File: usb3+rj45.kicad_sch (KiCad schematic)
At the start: 67 parts, among them J8 RJE361882415, T1 Trans_SM453229-381N7Y, T2 Trans_SM453229-381N7Y, T3 Trans_SM453229-381N7Y, T4 Trans_SM453229-381N7Y, T5 Choke_SRF2012A-801Y, T6 Choke_SRF2012A-801Y, T7 Choke_SRF2012A-801Y, T8 Choke_SRF2012A-801Y, U14 AP22615A_TSOT26, U15 ESD204DQAR, U16 ESD204DQAR, U17 AP22615A_TSOT26

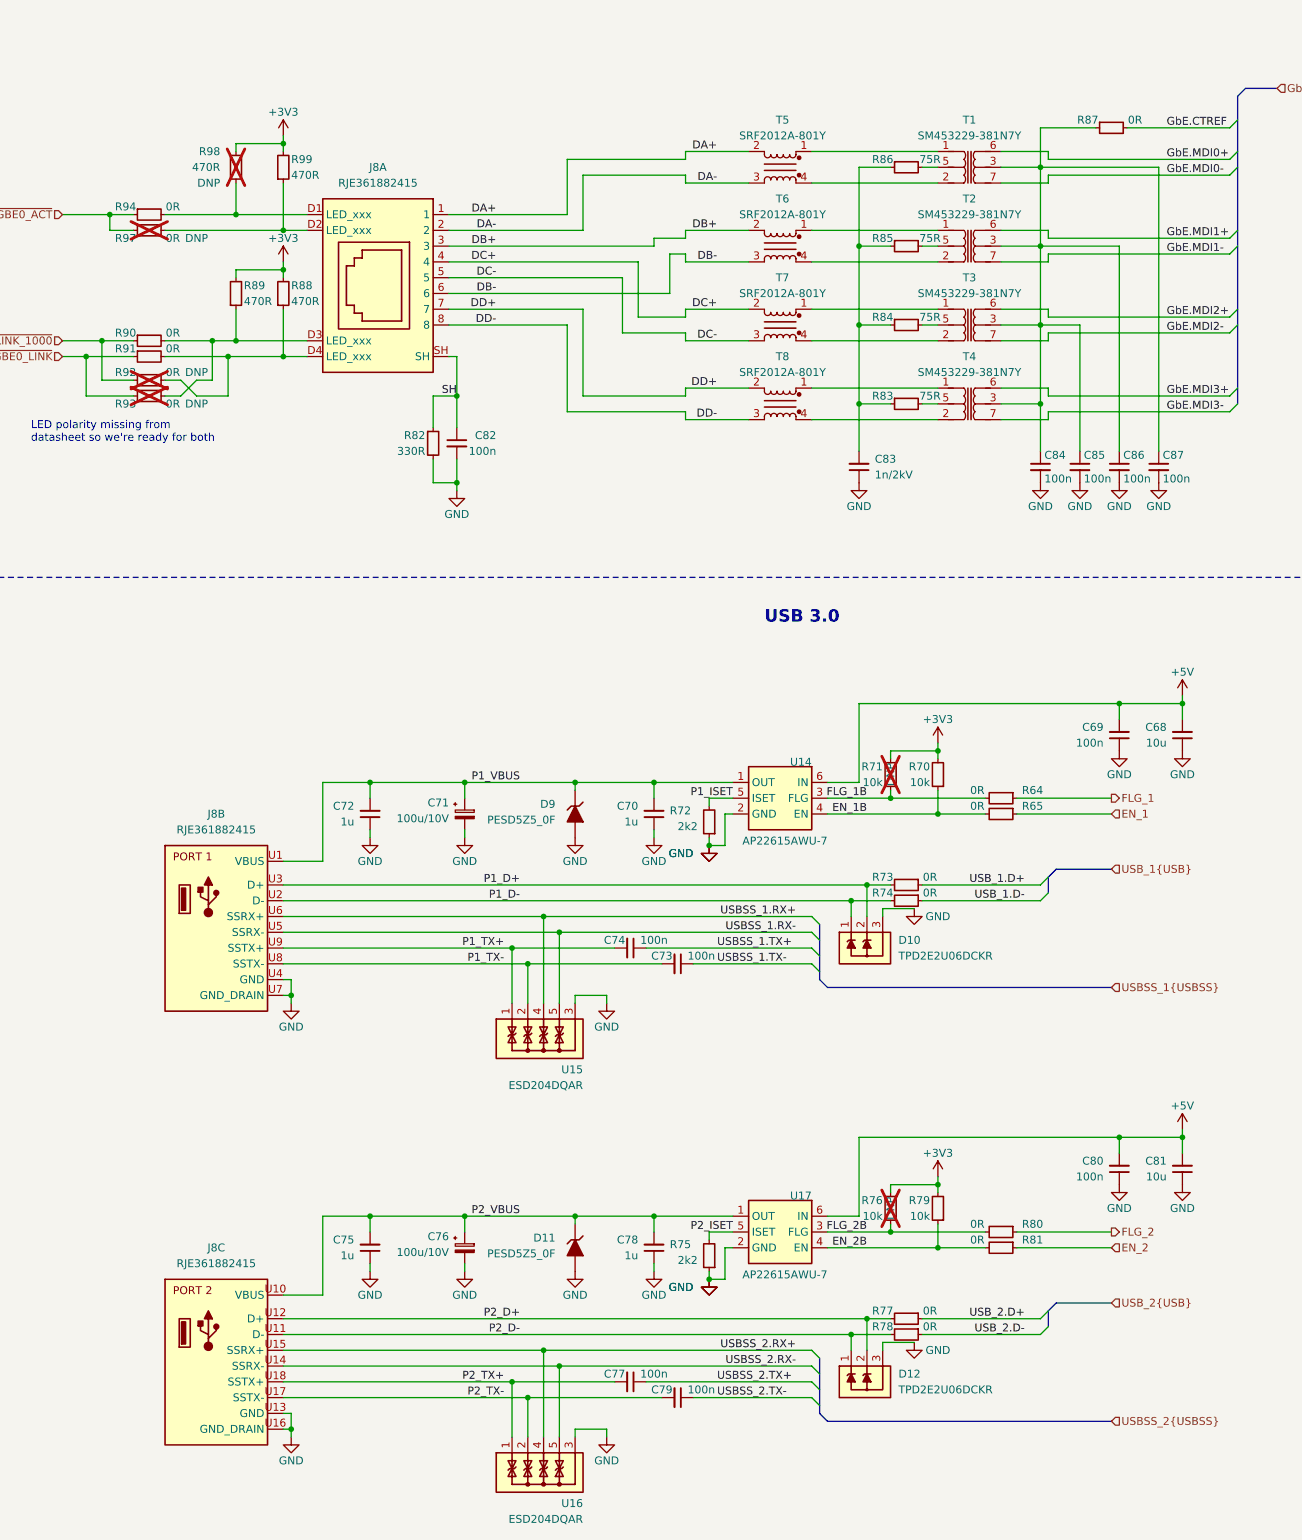
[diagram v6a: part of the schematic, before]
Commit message: [#58137] Update backplane connector pinout
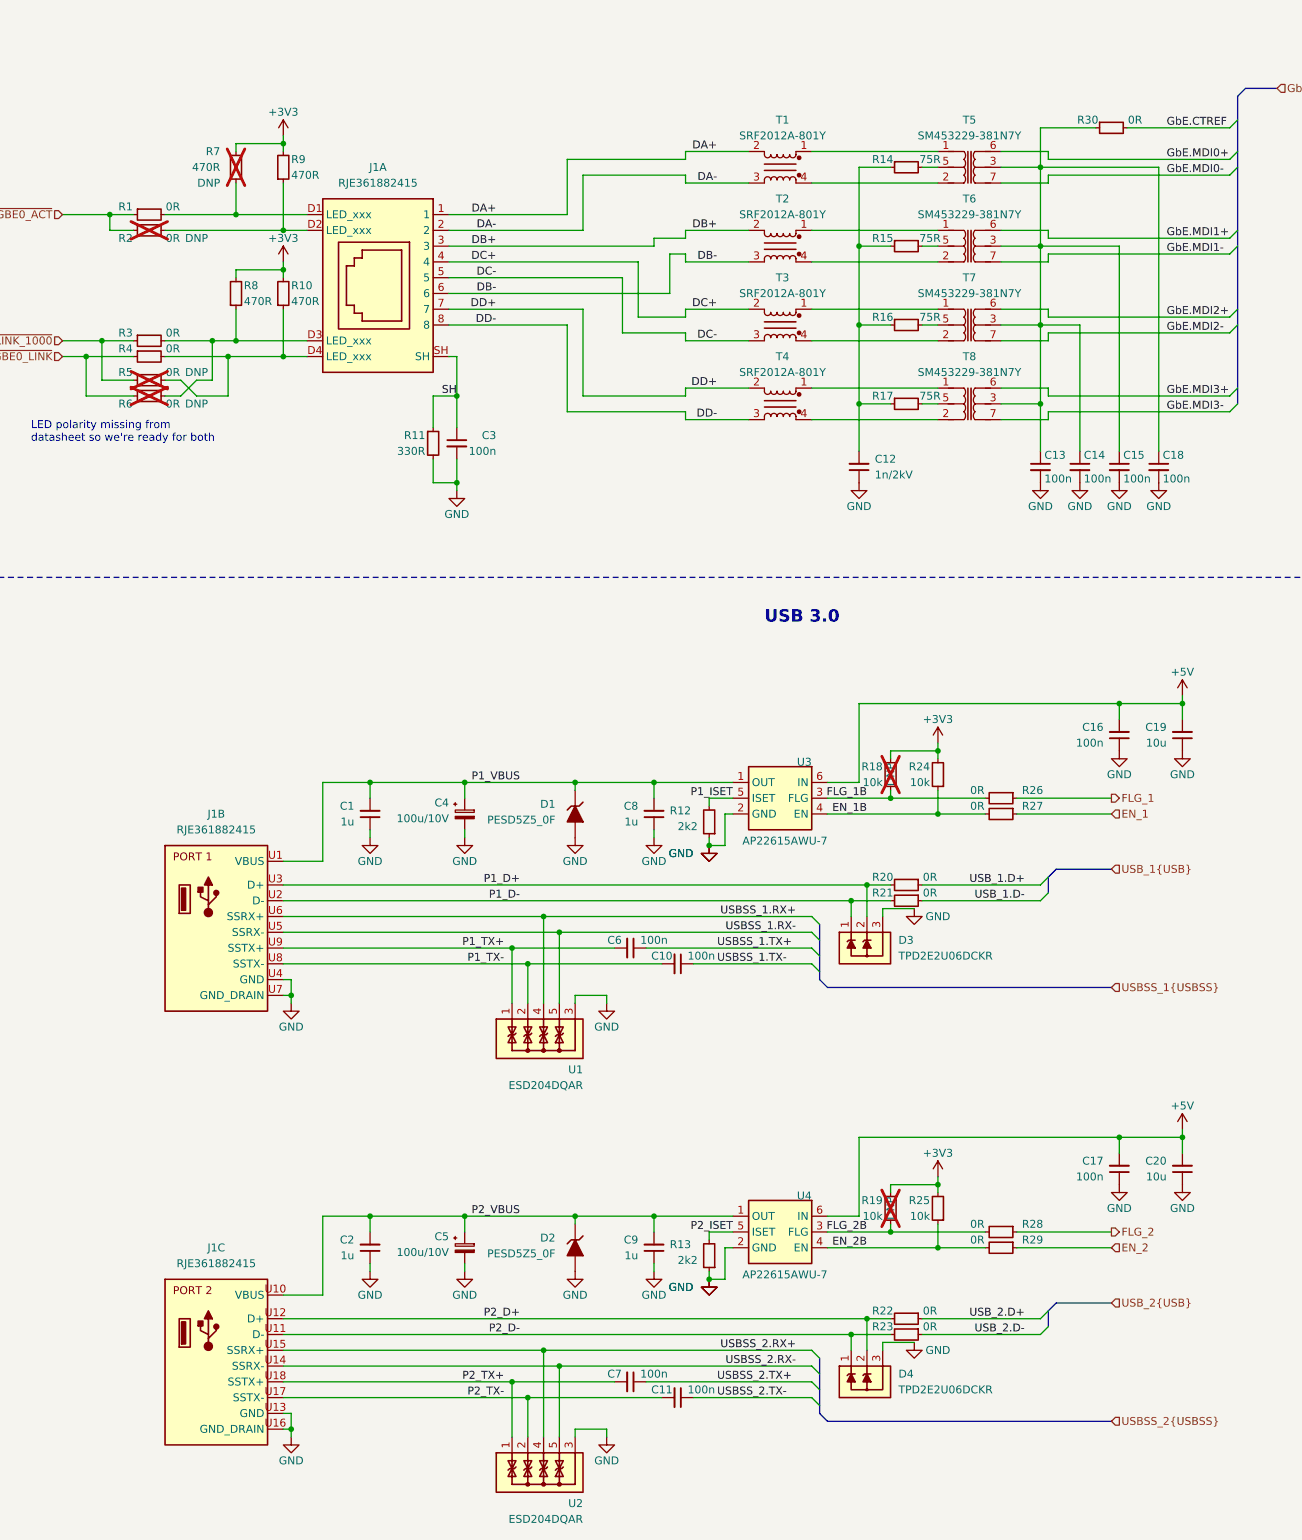
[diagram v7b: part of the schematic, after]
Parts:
- renumbered C72 to C1, C73 to C10, C79 to C11, C83 to C12, C84 to C13, C85 to C14, C86 to C15, C69 to C16, C80 to C17, C87 to C18, C68 to C19, C75 to C2, C81 to C20, C82 to C3, C71 to C4, C76 to C5, C74 to C6, C77 to C7, C70 to C8, C78 to C9, D9 to D1, D11 to D2, D10 to D3, D12 to D4, J8 to J1, R94 to R1, R88 to R10, R82 to R11, R72 to R12, R75 to R13, R86 to R14, R85 to R15, R84 to R16, R83 to R17, R71 to R18, R76 to R19, R97 to R2, R73 to R20, R74 to R21, R77 to R22, R78 to R23, R70 to R24, R79 to R25, R64 to R26, R65 to R27, R80 to R28, R81 to R29, R90 to R3, R87 to R30, R91 to R4, R92 to R5, R93 to R6, R98 to R7, R89 to R8, R99 to R9, T5 to T1, T6 to T2, T7 to T3, T8 to T4, T1 to T5, T2 to T6, T3 to T7, T4 to T8, U15 to U1, U16 to U2, U14 to U3, U17 to U4

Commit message: Update symbols from the library
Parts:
- J1: footprint (none) -> antmicro-footprints:RJ45_RJE361882415; Author (none) -> Antmicro; License (none) -> Apache-2.0
- T1, T2, T3, T4: footprint (none) -> antmicro-footprints:Choke_0805_2012Metric
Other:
- moved on the sheet: J1A, J1B, J1C, R1, R10, R2, R3, R4, R5, R6, R7, R8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
